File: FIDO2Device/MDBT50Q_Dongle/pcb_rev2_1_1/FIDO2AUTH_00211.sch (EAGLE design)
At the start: 36 parts, among them CN1 TE-1734028, CN2 IF_4PIN, CN3 IF_3PIN_SOL, CN4 IF_3PIN_SOL, SW1 SKRPACE010, SW2 SKTADAE010, U1 MDBT50Q-P1M, U2 XC6206P332MR-G, X1 NX3215SA-32.768K

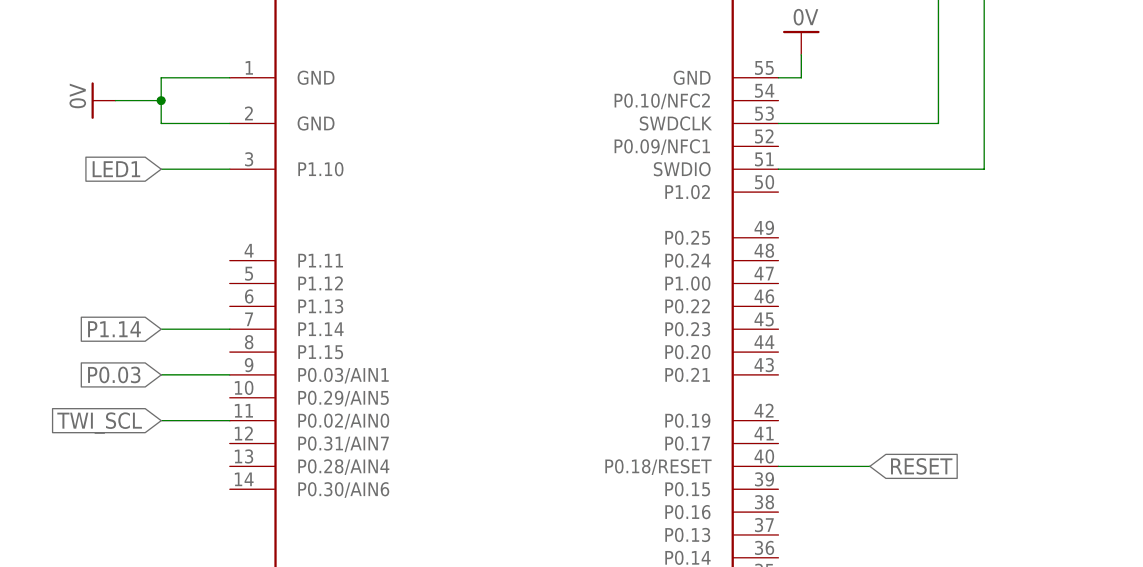
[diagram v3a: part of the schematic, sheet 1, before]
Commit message: プリント基板設計データを修正
・ATECC608Aの配置前の段階まで配線
・汎用I/Oを P0.25、P1.02 に変更
・TWI_SDA、TWI_SCL は表面に配置
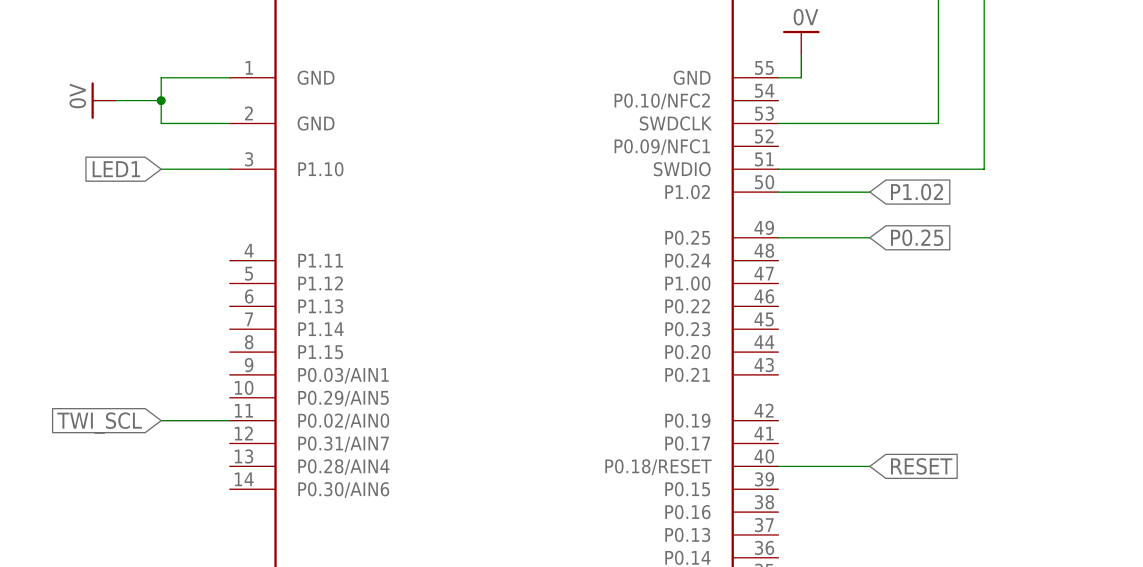
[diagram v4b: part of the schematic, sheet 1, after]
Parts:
- renumbered LED1 to LD1, LED2 to LD2, LED3 to LD3
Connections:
- removed net P0.03: CN4.3, U1.P0.03/AIN1
- removed net P1.14: CN4.2, U1.P1.14
- new net P0.25: CN4.3, U1.P0.25
- new net P1.02: CN4.2, U1.P1.02
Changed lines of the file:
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@@
 <setting verticaltext="up"/>
 </settings>
-<grid distance="0.1" unitdist="inch" unit="inch" style="lines" multiple="1" display="no" altdistance="0.01" altunitdist="inch" altunit="inch"/>
+<grid distance="0.1" unitdist="inch" unit="inch" style="lines" multiple="1" display="yes" altdistance="0.01" altunitdist="inch" altunit="inch"/>
 <layers>
 <layer number="1" name="Top" color="4" fill="1" visible="no" active="no"/>
@@
 <part name="SW2" library="Parts" deviceset="SKTADAE010" device=""/>
 <part name="GND12" library="Supply" deviceset="0V" device=""/>
-<part name="LED1" library="Parts" deviceset="APHD1608" device="LSURCK"/>
-<part name="LED2" library="Parts" deviceset="APHF1608" device="LSEEQBDZGKC"/>
+<part name="LD1" library="Parts" deviceset="APHD1608" device="LSURCK"/>
+<part name="LD2" library="Parts" deviceset="APHF1608" device="LSEEQBDZGKC"/>
 <part name="R2" library="Parts" deviceset="RESISTOR" device="_0402" value="1.5k"/>
 <part name="R3" library="Parts" deviceset="RESISTOR" device="_0402" value="1.2k"/>
@@
 <part name="CN3" library="Connectors" deviceset="IF_3PIN" device="_SOL" value="IF_3PIN_SOL"/>
 <part name="GND19" library="Supply" deviceset="0V" device=""/>
-<part name="LED3" library="Parts" deviceset="APTD1608" device="LSYCK"/>
+<part name="LD3" library="Parts" deviceset="APTD1608" device="LSYCK"/>
 <part name="R6" library="Parts" deviceset="RESISTOR" device="_0402" value="1.5k"/>
 <part name="FRAME4" library="Generic" deviceset="A4L-LOC" device=""/>
@@
 </segment>
 </net>
-<net name="P0.03" class="0">
-<segment>
-<pinref part="U1" gate="G$1" pin="P0.03/AIN1"/>
-<wire x1="43.18" y1="91.44" x2="35.56" y2="91.44" width="0.1524" layer="91"/>
-<label x="35.56" y="91.44" size="1.778" layer="95" rot="R180" xref="yes"/>
-</segment>
-</net>
-<net name="P1.14" class="0">
-<segment>
-<pinref part="U1" gate="G$1" pin="P1.14"/>
-<wire x1="43.18" y1="96.52" x2="35.56" y2="96.52" width="0.1524" layer="91"/>
-<label x="35.56" y="96.52" size="1.778" layer="95" rot="R180" xref="yes"/>
+<net name="P0.25" class="0">
+<segment>
+<pinref part="U1" gate="G$1" pin="P0.25"/>
+<wire x1="104.14" y1="106.68" x2="114.3" y2="106.68" width="0.1524" layer="91"/>
+<label x="114.3" y="106.68" size="1.778" layer="95" xref="yes"/>
+</segment>
+</net>
+<net name="P1.02" class="0">
+<segment>
+<pinref part="U1" gate="G$1" pin="P1.02"/>
+<wire x1="104.14" y1="111.76" x2="114.3" y2="111.76" width="0.1524" layer="91"/>
+<label x="114.3" y="111.76" size="1.778" layer="95" xref="yes"/>
 </segment>
 </net>
@@
 <instance part="D1" gate="G$1" x="114.3" y="124.46"/>
 <instance part="CN1" gate="G$1" x="30.48" y="124.46"/>
-<instance part="LED1" gate="G$1" x="33.02" y="60.96" smashed="yes">
+<instance part="LD1" gate="G$1" x="33.02" y="60.96" smashed="yes">
 <attribute name="NAME" x="36.576" y="58.928" size="1.778" layer="95"/>
 <attribute name="VALUE" x="36.195" y="56.388" size="1.778" layer="96"/>
 </instance>
-<instance part="LED2" gate="G$1" x="73.66" y="60.96"/>
+<instance part="LD2" gate="G$1" x="73.66" y="60.96"/>
 <instance part="R2" gate="G$1" x="33.02" y="40.64" rot="R90"/>
 <instance part="R3" gate="G$1" x="63.5" y="40.64" rot="R90"/>
@@
 <instance part="R5" gate="G$1" x="83.82" y="40.64" rot="R90"/>
 <instance part="GND14" gate="1" x="190.5" y="53.34"/>
-<instance part="LED3" gate="G$1" x="119.38" y="60.96" smashed="yes">
+<instance part="LD3" gate="G$1" x="119.38" y="60.96" smashed="yes">
 <attribute name="NAME" x="122.936" y="58.928" size="1.778" layer="95"/>
 <attribute name="VALUE" x="122.555" y="56.388" size="1.778" layer="96"/>
@@
 <net name="VDD_NRF" class="0">
 <segment>
-<pinref part="LED1" gate="G$1" pin="A"/>
+<pinref part="LD1" gate="G$1" pin="A"/>
 <wire x1="33.02" y1="63.5" x2="33.02" y2="68.58" width="0.1524" layer="91"/>
 <label x="33.02" y="68.58" size="1.778" layer="95" rot="R90" xref="yes"/>
 </segment>
 <segment>
-<pinref part="LED2" gate="G$1" pin="A"/>
+<pinref part="LD2" gate="G$1" pin="A"/>
 <wire x1="68.58" y1="63.5" x2="68.58" y2="68.58" width="0.1524" layer="91"/>
 <label x="68.58" y="68.58" size="1.778" layer="95" rot="R90" xref="yes"/>
@@
 </segment>
 <segment>
-<pinref part="LED3" gate="G$1" pin="A"/>
+<pinref part="LD3" gate="G$1" pin="A"/>
 <wire x1="119.38" y1="63.5" x2="119.38" y2="68.58" width="0.1524" layer="91"/>
 <label x="119.38" y="68.58" size="1.778" layer="95" rot="R90" xref="yes"/>
@@
 <net name="N$11" class="0">
 <segment>
-<pinref part="LED1" gate="G$1" pin="C"/>
+<pinref part="LD1" gate="G$1" pin="C"/>
 <pinref part="R2" gate="G$1" pin="2"/>
 <wire x1="33.02" y1="55.88" x2="33.02" y2="50.8" width="0.1524" layer="91"/>
@@
 <wire x1="63.5" y1="50.8" x2="63.5" y2="53.34" width="0.1524" layer="91"/>
 <wire x1="63.5" y1="53.34" x2="68.58" y2="53.34" width="0.1524" layer="91"/>
-<pinref part="LED2" gate="G$1" pin="CRED"/>
+<pinref part="LD2" gate="G$1" pin="CRED"/>
 <wire x1="68.58" y1="53.34" x2="68.58" y2="55.88" width="0.1524" layer="91"/>
 </segment>
@@
 <net name="N$6" class="0">
 <segment>
-<pinref part="LED2" gate="G$1" pin="CGREEN"/>
+<pinref part="LD2" gate="G$1" pin="CGREEN"/>
 <pinref part="R4" gate="G$1" pin="2"/>
 <wire x1="73.66" y1="55.88" x2="73.66" y2="50.8" width="0.1524" layer="91"/>
@@
 <net name="N$7" class="0">
 <segment>
-<pinref part="LED2" gate="G$1" pin="CBLUE"/>
+<pinref part="LD2" gate="G$1" pin="CBLUE"/>
 <wire x1="78.74" y1="55.88" x2="78.74" y2="53.34" width="0.1524" layer="91"/>
 <pinref part="R5" gate="G$1" pin="2"/>
@@
 <net name="N$8" class="0">
 <segment>
-<pinref part="LED3" gate="G$1" pin="C"/>
+<pinref part="LD3" gate="G$1" pin="C"/>
 <pinref part="R6" gate="G$1" pin="2"/>
 <wire x1="119.38" y1="55.88" x2="119.38" y2="50.8" width="0.1524" layer="91"/>
@@
 </segment>
 </net>
-<net name="P0.03" class="0">
+<net name="P0.25" class="0">
 <segment>
 <pinref part="CN4" gate="G$1" pin="3"/>
@@
 </segment>
 </net>
-<net name="P1.14" class="0">
+<net name="P1.02" class="0">
 <segment>
 <pinref part="CN4" gate="G$1" pin="2"/>

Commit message: プリント基板設計データを修正
・汎用I/OブレイクアウトからGNDを削除（不要なため）
・GNDパターンを改善
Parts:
- removed CN4: IF_3PIN_SOL, Connectors:IF_3PIN_SOL
- added CN5: IF_2PIN_SOL, Connectors:IF_2PIN_SOL
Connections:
- net 0V: no longer CN4.1
- net P0.25: now also CN5.2; no longer CN4.3
- net P1.02: now also CN5.1; no longer CN4.2
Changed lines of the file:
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@@
 <part name="R6" library="Parts" deviceset="RESISTOR" device="_0402" value="1.5k"/>
 <part name="FRAME4" library="Generic" deviceset="A4L-LOC" device=""/>
-<part name="CN4" library="Connectors" deviceset="IF_3PIN" device="_SOL" value="IF_3PIN_SOL"/>
-<part name="GND20" library="Supply" deviceset="0V" device=""/>
 <part name="CN2" library="Connectors" deviceset="IF_4PIN" device=""/>
+<part name="CN5" library="Connectors" deviceset="IF_2PIN" device="_SOL" value="IF_2PIN_SOL"/>
 </parts>
 <sheets>
@@
 <instance part="CN3" gate="G$1" x="203.2" y="68.58"/>
 <instance part="GND19" gate="1" x="195.58" y="55.88"/>
-<instance part="CN4" gate="G$1" x="203.2" y="116.84"/>
-<instance part="GND20" gate="1" x="195.58" y="104.14"/>
+<instance part="CN5" gate="G$1" x="203.2" y="111.76"/>
 </instances>
 <busses>
@@
 <wire x1="203.2" y1="63.5" x2="195.58" y2="63.5" width="0.1524" layer="91"/>
 <wire x1="195.58" y1="63.5" x2="195.58" y2="58.42" width="0.1524" layer="91"/>
-</segment>
-<segment>
-<pinref part="CN4" gate="G$1" pin="1"/>
-<wire x1="203.2" y1="111.76" x2="195.58" y2="111.76" width="0.1524" layer="91"/>
-<wire x1="195.58" y1="111.76" x2="195.58" y2="106.68" width="0.1524" layer="91"/>
-<pinref part="GND20" gate="1" pin="0V"/>
 </segment>
 </net>
@@
 <net name="P0.25" class="0">
 <segment>
-<pinref part="CN4" gate="G$1" pin="3"/>
-<wire x1="203.2" y1="116.84" x2="195.58" y2="116.84" width="0.1524" layer="91"/>
-<wire x1="195.58" y1="116.84" x2="195.58" y2="124.46" width="0.1524" layer="91"/>
-<label x="195.58" y="124.46" size="1.778" layer="95" rot="R90" xref="yes"/>
+<wire x1="195.58" y1="111.76" x2="195.58" y2="119.38" width="0.1524" layer="91"/>
+<label x="195.58" y="119.38" size="1.778" layer="95" rot="R90" xref="yes"/>
+<pinref part="CN5" gate="G$1" pin="2"/>
+<wire x1="203.2" y1="111.76" x2="195.58" y2="111.76" width="0.1524" layer="91"/>
 </segment>
 </net>
 <net name="P1.02" class="0">
 <segment>
-<pinref part="CN4" gate="G$1" pin="2"/>
-<wire x1="203.2" y1="114.3" x2="190.5" y2="114.3" width="0.1524" layer="91"/>
-<label x="190.5" y="114.3" size="1.778" layer="95" rot="R180" xref="yes"/>
-</segment>
-</net>
+<label x="190.5" y="109.22" size="1.778" layer="95" rot="R180" xref="yes"/>
+<pinref part="CN5" gate="G$1" pin="1"/>
+<wire x1="190.5" y1="109.22" x2="203.2" y2="109.22" width="0.1524" layer="91"/>
+</segment>
+</net>

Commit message: プリント基板設計データを修正
・TWIのブレイクアウトからGNDを削除（スペース削減のため）
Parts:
- CN3: value IF_3PIN_SOL -> IF_2PIN_SOL; device Connectors:IF_3PIN_SOL -> Connectors:IF_2PIN_SOL
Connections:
- net 0V: no longer CN3.1
- net TWI_SCL: now also CN3.1; no longer CN3.3
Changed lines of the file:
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@@
 <part name="BAT1" library="Connectors" deviceset="BAT-HLD-012-SMT" device=""/>
 <part name="GND18" library="Supply" deviceset="0V" device=""/>
-<part name="CN3" library="Connectors" deviceset="IF_3PIN" device="_SOL" value="IF_3PIN_SOL"/>
-<part name="GND19" library="Supply" deviceset="0V" device=""/>
 <part name="LD3" library="Parts" deviceset="APTD1608" device="LSYCK"/>
 <part name="R6" library="Parts" deviceset="RESISTOR" device="_0402" value="1.5k"/>
@@
 <part name="CN2" library="Connectors" deviceset="IF_4PIN" device=""/>
 <part name="CN5" library="Connectors" deviceset="IF_2PIN" device="_SOL" value="IF_2PIN_SOL"/>
+<part name="CN3" library="Connectors" deviceset="IF_2PIN" device="_SOL"/>
 </parts>
 <sheets>
@@
 <instance part="BAT1" gate="G$1" x="93.98" y="81.28"/>
 <instance part="GND18" gate="1" x="66.04" y="71.12"/>
+<instance part="CN5" gate="G$1" x="203.2" y="111.76"/>
 <instance part="CN3" gate="G$1" x="203.2" y="68.58"/>
-<instance part="GND19" gate="1" x="195.58" y="55.88"/>
-<instance part="CN5" gate="G$1" x="203.2" y="111.76"/>
 </instances>
 <busses>
@@
 <wire x1="88.9" y1="81.28" x2="66.04" y2="81.28" width="0.1524" layer="91"/>
 <wire x1="66.04" y1="81.28" x2="66.04" y2="73.66" width="0.1524" layer="91"/>
-</segment>
-<segment>
-<pinref part="CN3" gate="G$1" pin="1"/>
-<pinref part="GND19" gate="1" pin="0V"/>
-<wire x1="203.2" y1="63.5" x2="195.58" y2="63.5" width="0.1524" layer="91"/>
-<wire x1="195.58" y1="63.5" x2="195.58" y2="58.42" width="0.1524" layer="91"/>
 </segment>
 </net>
@@
 <net name="TWI_SDA" class="0">
 <segment>
-<pinref part="CN3" gate="G$1" pin="2"/>
-<wire x1="203.2" y1="66.04" x2="190.5" y2="66.04" width="0.1524" layer="91"/>
-<label x="190.5" y="66.04" size="1.778" layer="95" rot="R180" xref="yes"/>
-</segment>
-</net>
-<net name="TWI_SCL" class="0">
-<segment>
-<pinref part="CN3" gate="G$1" pin="3"/>
-<wire x1="203.2" y1="68.58" x2="195.58" y2="68.58" width="0.1524" layer="91"/>
 <wire x1="195.58" y1="68.58" x2="195.58" y2="76.2" width="0.1524" layer="91"/>
 <label x="195.58" y="76.2" size="1.778" layer="95" rot="R90" xref="yes"/>
-</segment>
-</net>
+<pinref part="CN3" gate="G$1" pin="2"/>
+<wire x1="203.2" y1="68.58" x2="195.58" y2="68.58" width="0.1524" layer="91"/>
+</segment>
+</net>
+<net name="TWI_SCL" class="0">
+<segment>
+<label x="190.5" y="66.04" size="1.778" layer="95" rot="R180" xref="yes"/>
+<pinref part="CN3" gate="G$1" pin="1"/>
+<wire x1="203.2" y1="66.04" x2="190.5" y2="66.04" width="0.1524" layer="91"/>
+</segment>
+</net>

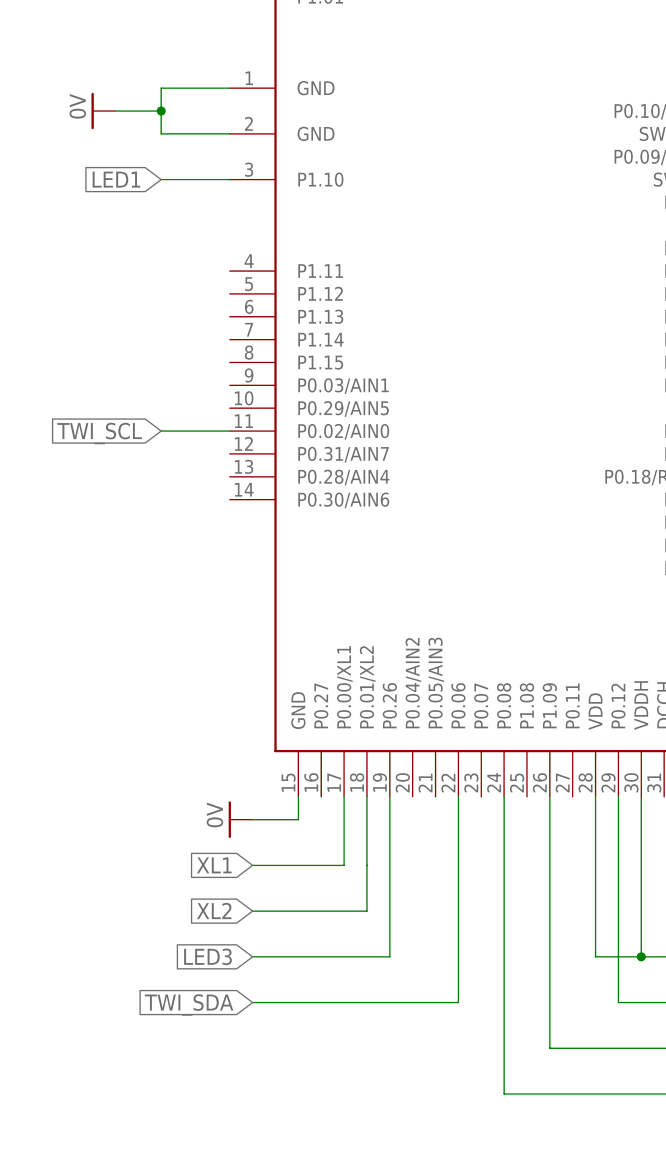
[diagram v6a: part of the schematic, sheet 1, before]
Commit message: プリント基板設計データを修正
・TWI関連の配線を改善するための措置
・SW1を基板の端に移動
・LED1の配線を、P1.10 --> P0.27 へ変更
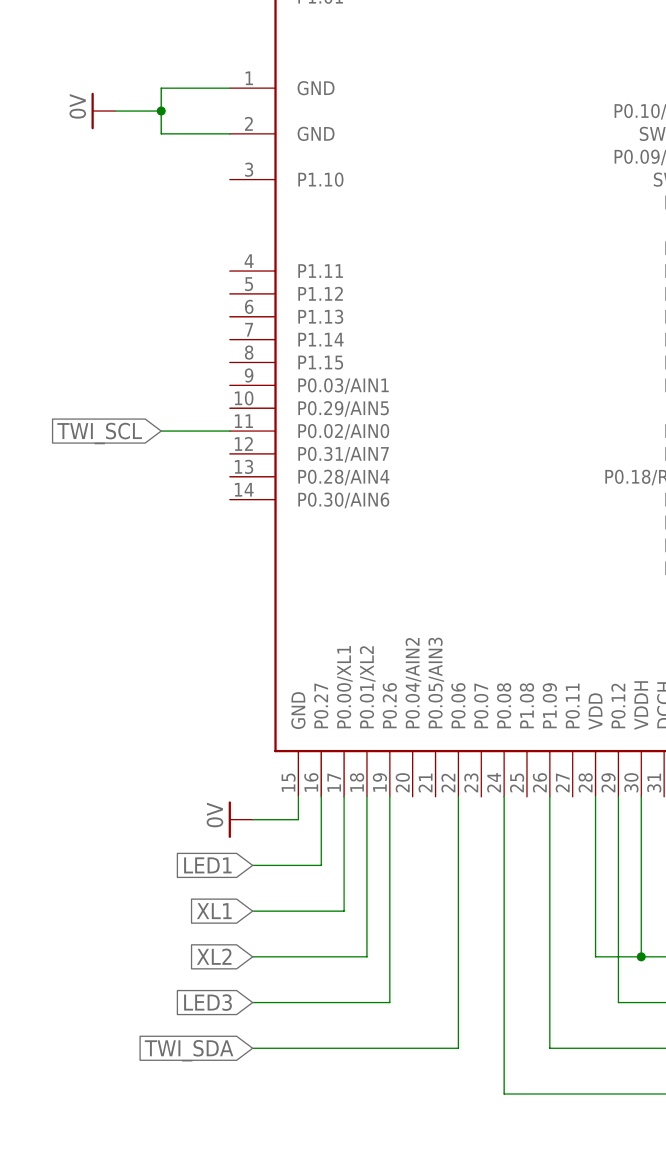
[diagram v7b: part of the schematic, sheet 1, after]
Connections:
- net LED1: now also U1.P0.27; no longer U1.P1.10
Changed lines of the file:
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@@
 <segment>
 <pinref part="U1" gate="G$1" pin="P0.00/XL1"/>
-<wire x1="55.88" y1="45.72" x2="55.88" y2="38.1" width="0.1524" layer="91"/>
-<wire x1="55.88" y1="38.1" x2="45.72" y2="38.1" width="0.1524" layer="91"/>
-<label x="45.72" y="38.1" size="1.778" layer="95" rot="R180" xref="yes"/>
+<wire x1="55.88" y1="45.72" x2="55.88" y2="33.02" width="0.1524" layer="91"/>
+<wire x1="55.88" y1="33.02" x2="45.72" y2="33.02" width="0.1524" layer="91"/>
+<label x="45.72" y="33.02" size="1.778" layer="95" rot="R180" xref="yes"/>
 </segment>
 </net>
@@
 <segment>
 <pinref part="U1" gate="G$1" pin="P0.01/XL2"/>
-<wire x1="58.42" y1="45.72" x2="58.42" y2="38.1" width="0.1524" layer="91"/>
-<wire x1="58.42" y1="38.1" x2="58.42" y2="33.02" width="0.1524" layer="91"/>
-<wire x1="58.42" y1="33.02" x2="45.72" y2="33.02" width="0.1524" layer="91"/>
-<label x="45.72" y="33.02" size="1.778" layer="95" rot="R180" xref="yes"/>
+<wire x1="58.42" y1="45.72" x2="58.42" y2="27.94" width="0.1524" layer="91"/>
+<wire x1="58.42" y1="27.94" x2="45.72" y2="27.94" width="0.1524" layer="91"/>
+<label x="45.72" y="27.94" size="1.778" layer="95" rot="R180" xref="yes"/>
 </segment>
 </net>
@@
 <segment>
 <pinref part="U1" gate="G$1" pin="P0.06"/>
-<wire x1="68.58" y1="45.72" x2="68.58" y2="22.86" width="0.1524" layer="91"/>
-<wire x1="68.58" y1="22.86" x2="45.72" y2="22.86" width="0.1524" layer="91"/>
-<label x="45.72" y="22.86" size="1.778" layer="95" rot="R180" xref="yes"/>
+<wire x1="68.58" y1="45.72" x2="68.58" y2="17.78" width="0.1524" layer="91"/>
+<wire x1="68.58" y1="17.78" x2="45.72" y2="17.78" width="0.1524" layer="91"/>
+<label x="45.72" y="17.78" size="1.778" layer="95" rot="R180" xref="yes"/>
 </segment>
 </net>
 <net name="LED1" class="0">
 <segment>
-<pinref part="U1" gate="G$1" pin="P1.10"/>
-<wire x1="43.18" y1="114.3" x2="35.56" y2="114.3" width="0.1524" layer="91"/>
-<label x="35.56" y="114.3" size="1.778" layer="95" rot="R180" xref="yes"/>
+<label x="45.72" y="38.1" size="1.778" layer="95" rot="R180" xref="yes"/>
+<pinref part="U1" gate="G$1" pin="P0.27"/>
+<wire x1="53.34" y1="45.72" x2="53.34" y2="38.1" width="0.1524" layer="91"/>
+<wire x1="53.34" y1="38.1" x2="45.72" y2="38.1" width="0.1524" layer="91"/>
 </segment>
 </net>
@@
 <segment>
 <pinref part="U1" gate="G$1" pin="P0.26"/>
-<wire x1="60.96" y1="45.72" x2="60.96" y2="27.94" width="0.1524" layer="91"/>
-<wire x1="60.96" y1="27.94" x2="45.72" y2="27.94" width="0.1524" layer="91"/>
-<label x="45.72" y="27.94" size="1.778" layer="95" rot="R180" xref="yes"/>
+<wire x1="60.96" y1="45.72" x2="60.96" y2="22.86" width="0.1524" layer="91"/>
+<wire x1="60.96" y1="22.86" x2="45.72" y2="22.86" width="0.1524" layer="91"/>
+<label x="45.72" y="22.86" size="1.778" layer="95" rot="R180" xref="yes"/>
 </segment>
 </net>
